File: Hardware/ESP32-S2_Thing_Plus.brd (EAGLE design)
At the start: 22.9 x 66 mm, 121 parts, among them J3 QWIIC_RA, J5 USB-C, J6 JTAG, Q1 2.5A/30V, Q2 MBT3904DW1T1, U1 MCP73831, U2 ESP32-S2-WROOM, U3 AP2112K-3.3V, U4 CP210X, Y1 32.768kHz

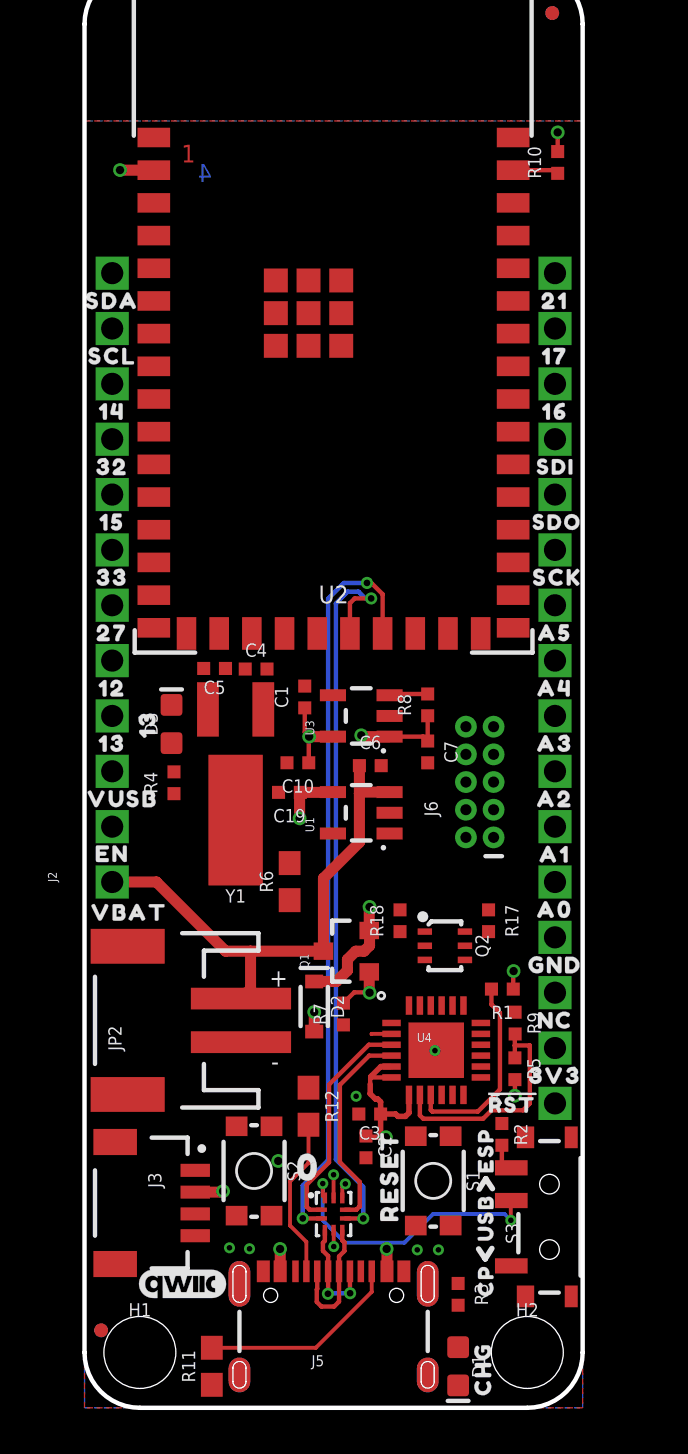
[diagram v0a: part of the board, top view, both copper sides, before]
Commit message: added charge current jumper options and did a bunch of routing
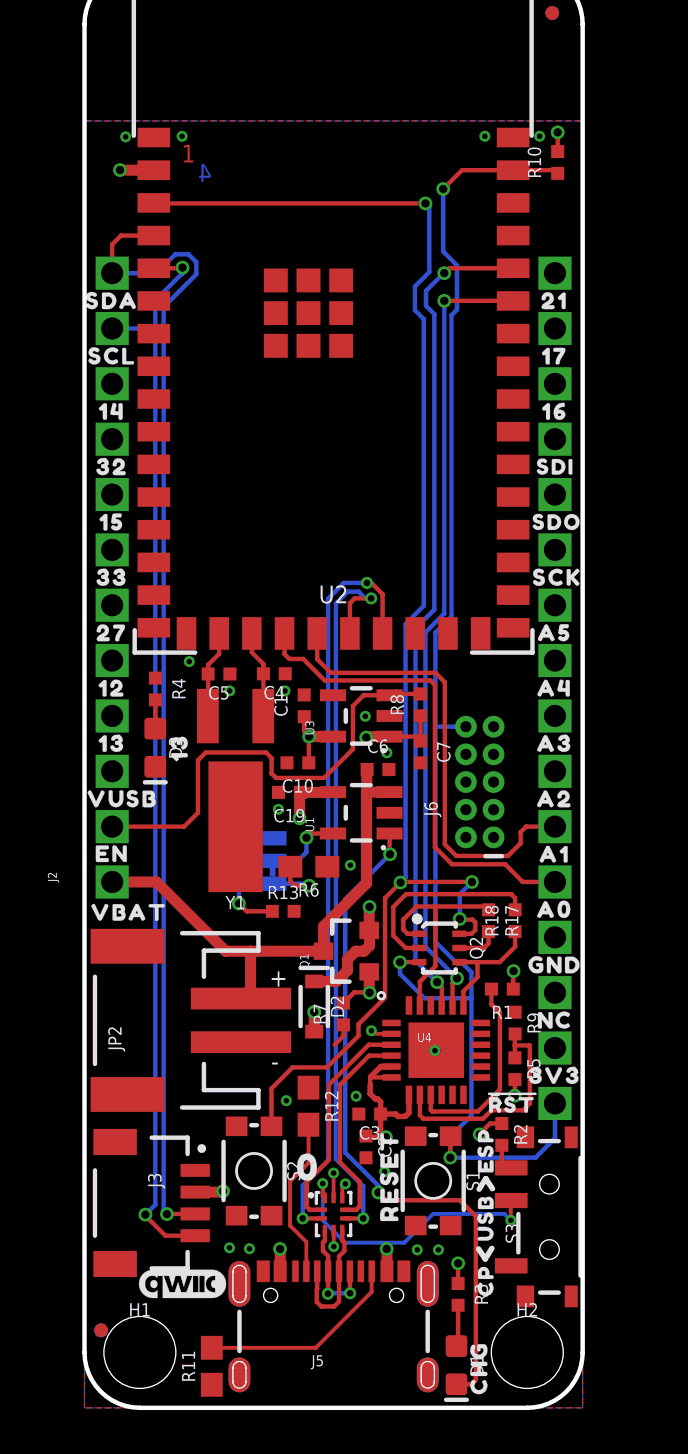
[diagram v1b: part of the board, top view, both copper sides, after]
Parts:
- added CHG: (no value), SparkFun-Jumpers:SMT-JUMPER_3_1-NC_TRACE_SILK
- added R13: 10k, SparkFun-Resistors:0402-TIGHT
- TP1: value TEST-POINTTP_15TH_THRU -> (none)
- moved TP1 15.6 mm to (17.8, 24.1)
- moved R18 5.28 mm to (19.8, 22.4)
- moved R4 4.38 mm to (3.26, 33.0), turned to 270 degrees
- moved U$74 1.82 mm to (4.36, 30.3)
- moved D3 1.32 mm to (3.25, 30.3), turned to 270 degrees
- moved R6 1.12 mm to (10.3, 24.8), turned to 180 degrees
- moved C4 0.87 mm to (8.71, 33.7), turned to 180 degrees
- moved C1 0.41 mm to (10.1, 32.2)
- moved C6 0.40 mm to (13.5, 29.3)
- moved C7 0.33 mm to (15.4, 30.1)
- moved R8 0.33 mm to (15.4, 32.3)
- moved C5 0.33 mm to (6.17, 33.7)
- moved Y1 0.30 mm to (6.93, 31.7)
- moved Q2 0.27 mm to (16.3, 21.1)
- moved U$78 0.18 mm to (18.1, 1.83)
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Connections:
- removed net N$14: R6.2, U1.5
- new net N$11: CHG.1, R13.1
- new net N$13: CHG.3, R6.2
- new net N$9: CHG.2, U1.5
- net GND: now also R13.2
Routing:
- net 0: track 0.00 -> 66.3 mm, vias 0 -> 3
- net CHIP_PU: track 2.10 -> 66.4 mm, vias 0 -> 3
- net SDA: track 0.00 -> 53.4 mm, vias 0 -> 1
- net SCL: track 0.00 -> 50.2 mm, vias 0 -> 2
- net TX: track 0.00 -> 38.2 mm, vias 0 -> 2
- net RX: track 0.00 -> 36.5 mm, vias 0 -> 2
- net CHG: track 0.00 -> 31.4 mm, vias 0 -> 2
- net A0: track 0.00 -> 22.1 mm
- net A1: track 0.00 -> 21.0 mm
- net EN: track 1.77 -> 20.6 mm
- net DTR: track 0.00 -> 10.3 mm
- net N$12: track 0.00 -> 9.19 mm
- net V_USB: track 14.4 -> 20.5 mm, vias 6 -> 7
- net N$11: track 0.00 -> 5.88 mm, vias 0 -> 1
- net RTS: track 0.00 -> 5.80 mm
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
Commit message: Moved to smaller/newer 32.768kHz crystal
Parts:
- C4, C5: value 22pF -> 15pF
- Y1: device SparkFun-Clocks:CRYSTAL-SMD-2X6-CYL -> SparkFun-Clocks:CRYSTAL-SMD-3.2X1.5MM
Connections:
- net N$7: now also Y1.P$2; no longer Y1.X2
- net N$8: now also Y1.P$1; no longer Y1.X1
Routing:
- net EN: track 20.6 -> 17.8 mm
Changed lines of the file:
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@@
 <setting verticaltext="up"/>
 </settings>
-<grid distance="0.05" unitdist="inch" unit="inch" style="lines" multiple="1" display="yes" altdistance="0.001" altunitdist="inch" altunit="inch"/>
+<grid distance="0.05" unitdist="inch" unit="inch" style="lines" multiple="1" display="yes" altdistance="0.005" altunitdist="inch" altunit="inch"/>
 <layers>
 <layer number="1" name="Top" color="4" fill="1" visible="yes" active="yes"/>
 <layer number="2" name="Route2" color="1" fill="3" visible="no" active="yes"/>
 <layer number="15" name="Route15" color="4" fill="6" visible="no" active="yes"/>
-<layer number="16" name="Bottom" color="1" fill="1" visible="yes" active="yes"/>
+<layer number="16" name="Bottom" color="1" fill="1" visible="no" active="yes"/>
 <layer number="17" name="Pads" color="2" fill="1" visible="yes" active="yes"/>
 <layer number="18" name="Vias" color="2" fill="1" visible="yes" active="yes"/>
 <layer number="19" name="Unrouted" color="6" fill="1" visible="yes" active="yes"/>
 <layer number="20" name="Dimension" color="24" fill="1" visible="yes" active="yes"/>
-<layer number="21" name="tPlace" color="16" fill="1" visible="no" active="yes"/>
+<layer number="21" name="tPlace" color="16" fill="1" visible="yes" active="yes"/>
 <layer number="22" name="bPlace" color="14" fill="1" visible="no" active="yes"/>
 <layer number="23" name="tOrigins" color="15" fill="1" visible="yes" active="yes"/>
@@
 <layer number="47" name="Measures" color="7" fill="1" visible="no" active="yes"/>
 <layer number="48" name="Document" color="7" fill="1" visible="no" active="yes"/>
-<layer number="49" name="Reference" color="7" fill="1" visible="yes" active="yes"/>
-<layer number="51" name="tDocu" color="6" fill="1" visible="no" active="yes"/>
+<layer number="49" name="Reference" color="7" fill="1" visible="no" active="yes"/>
+<layer number="51" name="tDocu" color="6" fill="1" visible="yes" active="yes"/>
 <layer number="52" name="bDocu" color="7" fill="1" visible="no" active="yes"/>
 <layer number="3" name="Route3" color="4" fill="3" visible="no" active="no"/>
@@
 <attribute name="VALUE" x="22.733" y="8.763" size="0.6096" layer="27" font="vector" ratio="20" rot="R90" align="top-center"/>
 </element>
-<element name="Y1" library="SparkFun-Clocks" package="CRYSTAL-SMD-2X6-CYL" value="32.768kHz" x="6.934196875" y="31.74491875" smashed="yes" rot="R180">
+<element name="Y1" library="SparkFun-Clocks" package="CRYSTAL-SMD-3.2X1.5MM" value="32.768kHz" x="6.934196875" y="31.74491875" smashed="yes" rot="R180">
 <attribute name="NAME" x="6.934196875" y="23.48991875" size="0.6096" layer="25" font="vector" ratio="20" rot="R180" align="bottom-center"/>
-<attribute name="PROD_ID" value="XTAL-07894" x="6.934196875" y="31.74491875" size="1.778" layer="27" font="vector" ratio="15" rot="R180" display="off"/>
+<attribute name="PROD_ID" value="XTAL-13062" x="6.934196875" y="31.74491875" size="1.778" layer="27" font="vector" ratio="15" rot="R180" display="off"/>
 <attribute name="VALUE" x="6.934196875" y="33.26891875" size="0.6096" layer="27" font="vector" ratio="20" rot="R180" align="top-center"/>
 </element>
@@
 <attribute name="VALUE" value="10k" x="18.5896" y="12.5476" size="0.6096" layer="27" font="vector" ratio="20" rot="R270" align="top-center"/>
 </element>
-<element name="C4" library="SparkFun-Capacitors" package="0402-TIGHT" value="22pF" x="8.712203125" y="33.68548125" smashed="yes" rot="R180">
+<element name="C4" library="SparkFun-Capacitors" package="0402-TIGHT" value="15pF" x="8.712203125" y="33.68548125" smashed="yes" rot="R180">
 <attribute name="NAME" x="8.712203125" y="33.12348125" size="0.6096" layer="25" font="vector" ratio="20" rot="R180" align="bottom-center"/>
-<attribute name="PROD_ID" value="CAP-14674" x="8.712203125" y="33.68548125" size="1.778" layer="27" font="vector" ratio="15" rot="R180" display="off"/>
-<attribute name="VALUE" x="8.712203125" y="34.24748125" size="0.6096" layer="27" font="vector" ratio="20" rot="R180" align="top-center"/>
-</element>
-<element name="C5" library="SparkFun-Capacitors" package="0402-TIGHT" value="22pF" x="6.172196875" y="33.67531875" smashed="yes" rot="R180">
+<attribute name="PROD_ID" value="CAP-13063" x="8.712203125" y="33.68548125" size="1.778" layer="27" font="vector" ratio="15" rot="R180" display="off"/>
+<attribute name="VALUE" value="15pF" x="8.712203125" y="34.24748125" size="0.6096" layer="27" font="vector" ratio="20" rot="R180" align="top-center"/>
+</element>
+<element name="C5" library="SparkFun-Capacitors" package="0402-TIGHT" value="15pF" x="6.172196875" y="33.67531875" smashed="yes" rot="R180">
 <attribute name="NAME" x="6.172196875" y="33.11331875" size="0.6096" layer="25" font="vector" ratio="20" rot="R180" align="bottom-center"/>
-<attribute name="PROD_ID" value="CAP-14674" x="6.172196875" y="33.67531875" size="1.778" layer="27" font="vector" ratio="15" rot="R180" display="off"/>
-<attribute name="VALUE" x="6.172196875" y="34.23731875" size="0.6096" layer="27" font="vector" ratio="20" rot="R180" align="top-center"/>
+<attribute name="PROD_ID" value="CAP-13063" x="6.172196875" y="33.67531875" size="1.778" layer="27" font="vector" ratio="15" rot="R180" display="off"/>
+<attribute name="VALUE" value="15pF" x="6.172196875" y="34.23731875" size="0.6096" layer="27" font="vector" ratio="20" rot="R180" align="top-center"/>
 </element>
 <element name="R11" library="SparkFun-Resistors" package="0603" value="5.1k" x="5.842" y="1.905" smashed="yes" rot="R90">
@@
 <wire x1="12.319" y1="32.2072" x2="12.319" y2="30.226" width="0.2032" layer="1"/>
 <wire x1="12.319" y1="30.226" x2="10.9982" y2="28.9052" width="0.2032" layer="1"/>
-<wire x1="8.7884" y1="28.9052" x2="8.5852" y2="29.1084" width="0.2032" layer="1"/>
-<wire x1="8.5852" y1="29.8196" x2="8.3312" y2="30.0736" width="0.2032" layer="1"/>
-<wire x1="8.3312" y1="30.0736" x2="5.5626" y2="30.0736" width="0.2032" layer="1"/>
-<wire x1="5.207" y1="29.718" x2="5.207" y2="27.305" width="0.2032" layer="1"/>
-<wire x1="5.207" y1="27.305" x2="4.572" y2="26.67" width="0.2032" layer="1"/>
-<wire x1="4.572" y1="26.67" x2="1.27" y2="26.67" width="0.2032" layer="1"/>
+<wire x1="2.286" y1="26.67" x2="1.27" y2="26.67" width="0.2032" layer="1"/>
 <wire x1="12.8118" y1="32.7" x2="12.319" y2="32.2072" width="0.2032" layer="1"/>
-<wire x1="10.9982" y1="28.9052" x2="8.7884" y2="28.9052" width="0.2032" layer="1"/>
-<wire x1="8.5852" y1="29.1084" x2="8.5852" y2="29.8196" width="0.2032" layer="1"/>
-<wire x1="5.5626" y1="30.0736" x2="5.207" y2="29.718" width="0.2032" layer="1"/>
+<wire x1="4.5212" y1="28.9052" x2="2.286" y2="26.67" width="0.2032" layer="1"/>
+<wire x1="10.9982" y1="28.9052" x2="4.5212" y2="28.9052" width="0.2032" layer="1"/>
 </signal>
 <signal name="N$2">
@@
 <signal name="N$7">
 <contactref element="U2" pad="18"/>
-<contactref element="Y1" pad="X2"/>
+<contactref element="Y1" pad="P$2"/>
 <contactref element="C5" pad="2"/>
 <wire x1="6.18" y1="35.535" x2="6.18" y2="34.6026" width="0.2032" layer="1"/>
@@
 <wire x1="6.18" y1="34.6026" x2="5.672196875" y2="34.094796875" width="0.2032" layer="1"/>
 <wire x1="5.672196875" y1="33.67531875" x2="5.672196875" y2="31.75291875" width="0.2032" layer="1"/>
-<wire x1="5.672196875" y1="31.75291875" x2="5.664196875" y2="31.74491875" width="0.2032" layer="1"/>
+<wire x1="5.672196875" y1="31.75291875" x2="5.684196875" y2="31.74491875" width="0" layer="19" extent="1-1"/>
 </signal>
 <signal name="N$8">
 <contactref element="U2" pad="19"/>
-<contactref element="Y1" pad="X1"/>
+<contactref element="Y1" pad="P$1"/>
 <contactref element="C4" pad="2"/>
 <wire x1="7.68" y1="35.535" x2="7.68" y2="34.6618" width="0.2032" layer="1"/>
@@
 <wire x1="7.68" y1="34.6618" x2="8.212203125" y2="34.129596875" width="0.2032" layer="1"/>
 <wire x1="8.212203125" y1="33.68548125" x2="8.212203125" y2="31.752925" width="0.2032" layer="1"/>
-<wire x1="8.212203125" y1="31.752925" x2="8.204196875" y2="31.74491875" width="0.2032" layer="1"/>
+<wire x1="8.212203125" y1="31.752925" x2="8.184196875" y2="31.74491875" width="0" layer="19" extent="1-1"/>
 </signal>
 <signal name="CC2">

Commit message: moving vreg in progress
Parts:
- moved R8 14.0 mm to (3.00, 25.8), turned to 270 degrees
- moved C7 11.7 mm to (5.49, 24.0), turned to 180 degrees
- moved U3 8.92 mm to (5.87, 26.0), turned to 270 degrees
- moved C1 5.54 mm to (5.77, 28.7), turned to 0 degrees
- moved C10 4.02 mm to (5.78, 29.8), turned to 0 degrees
- moved C19 1.81 mm to (10.9, 29.3)
- moved R13 1.20 mm to (10.3, 23.1)
- moved CHG 0.41 mm to (9.04, 25.1)
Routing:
- net EN: track 17.8 -> 4.59 mm
- net VIN: track 16.9 -> 20.5 mm
- net 3.3V: track 29.7 -> 26.5 mm
- net V_BATT: track 23.6 -> 26.6 mm
- net GND: vias 22 -> 23

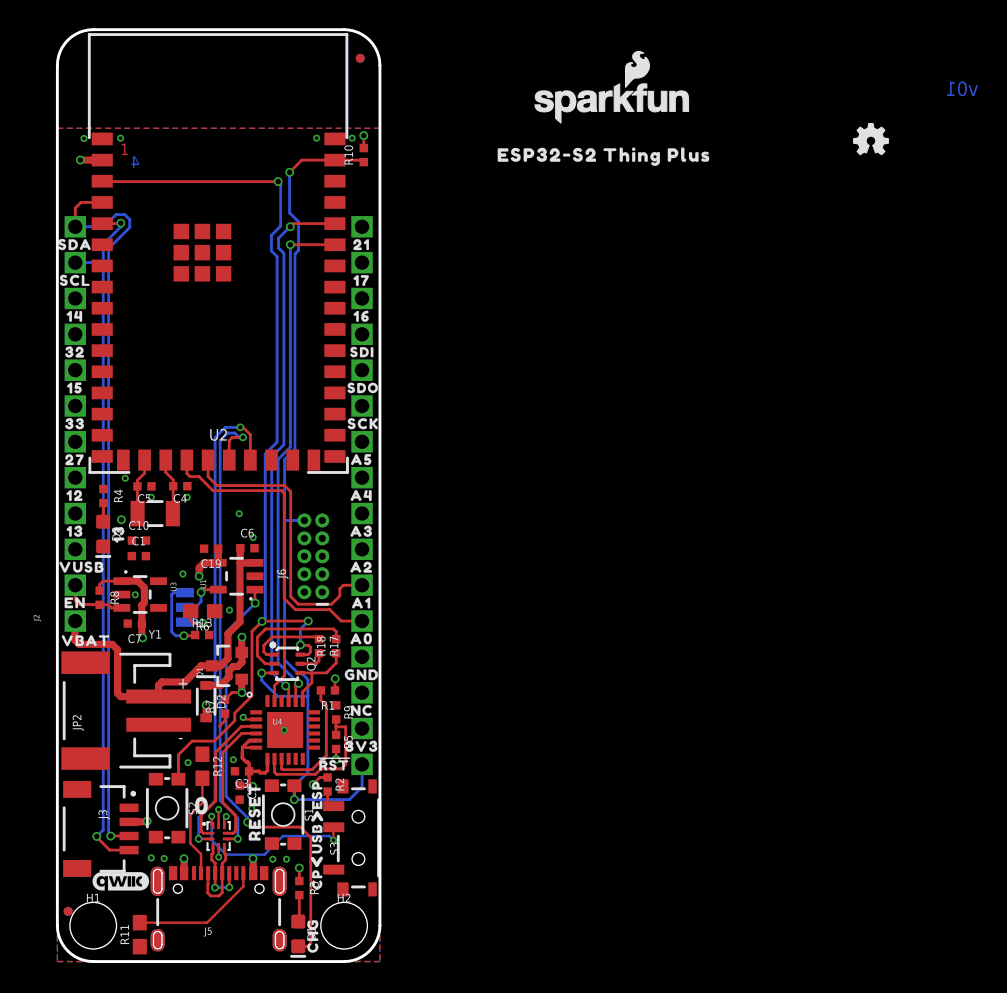
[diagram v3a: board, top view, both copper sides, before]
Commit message: All IO (except "extra SMD IO") routed
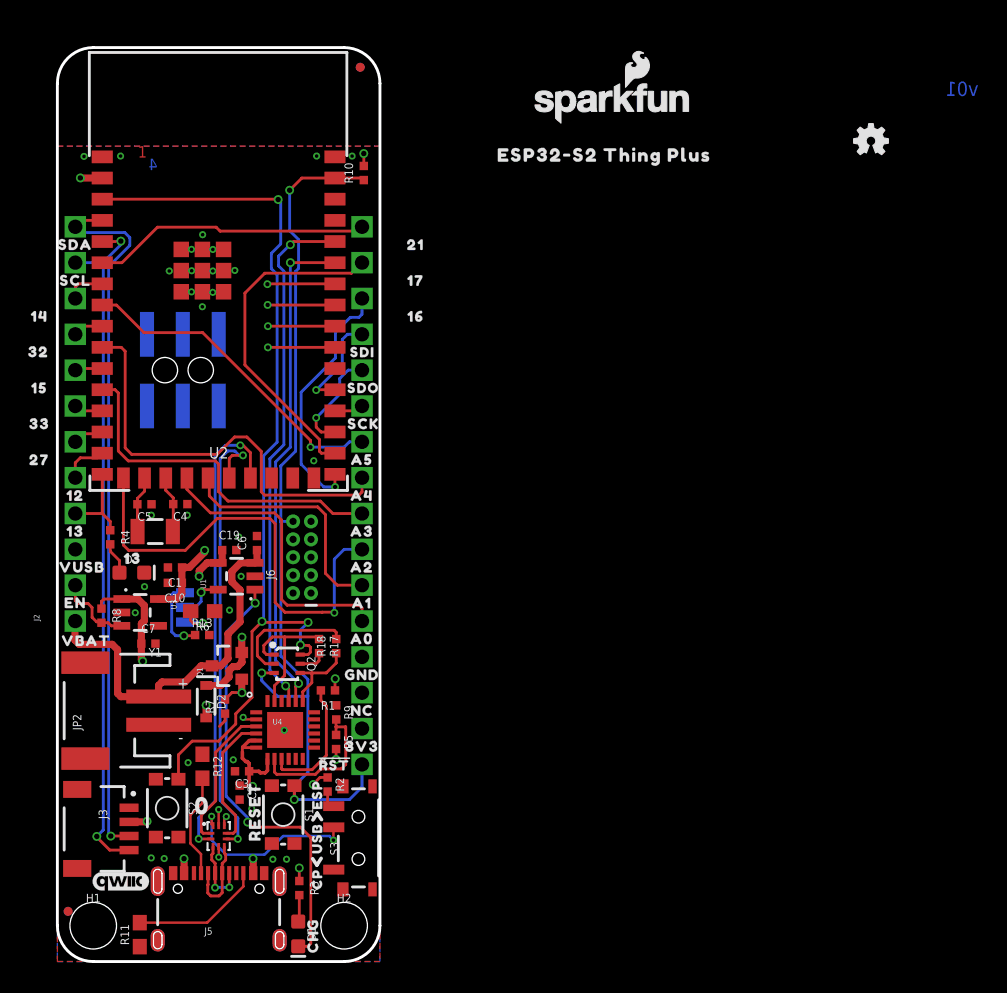
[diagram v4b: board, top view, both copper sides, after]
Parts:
- added J1: (no value), SparkFun-Connectors:2X3_SMT_POSTS
- moved U$31 8.89 mm to (-7.11, 52.1)
- moved U$33 8.89 mm to (-7.11, 49.5)
- moved U$4 8.89 mm to (30.0, 49.5)
- moved U$5 8.89 mm to (30.0, 47.0)
- moved U$3 6.35 mm to (27.4, 52.1)
- moved U$34 5.08 mm to (-3.30, 47.0)
- moved U$35 5.08 mm to (-3.30, 44.5)
- moved U$36 5.08 mm to (-3.30, 41.9)
- moved U$37 5.08 mm to (-3.30, 39.4)
- moved U$38 5.08 mm to (-3.30, 36.8)
- moved C10 3.93 mm to (8.32, 26.8), turned to 180 degrees
- moved U$93 3.81 mm to (25.4, 45.7)
- moved U$94 3.81 mm to (25.4, 48.3)
- moved U$95 3.81 mm to (25.4, 50.8)
- moved D3 3.41 mm to (5.28, 27.6), turned to 0 degrees
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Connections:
- new net 10: J2.7, U2.13
- new net 11: J2.6, U2.14
- new net 12: J2.5, U2.15
- new net 21: U2.24
- new net 26: U2.25
- new net 3: J4.16, U2.6
- new net 33: J4.14, U2.27
- new net 34: J4.15, U2.28
- new net 38: U2.32
- new net 4: J2.10, U2.7
- new net 45: U2.39
- new net 46: U2.40
- new net 6: J2.9, U2.9
- new net 8: J2.8, U2.11
- new net N$14: J1.2
- new net N$15: J1.4
- new net N$16: J1.6
- new net N$18: J1.1
- new net N$19: J1.3
- new net N$20: J1.5
- net 13: now also J2.4, U2.16
- net A2: now also U2.17
- net A3: now also U2.12
- net A4: now also U2.10
- net A5: now also U2.8
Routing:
- net A2: track 0.00 -> 32.9 mm, vias 0 -> 1
- net A4: track 0.00 -> 30.6 mm
- net MTMS: track 0.00 -> 28.0 mm, vias 0 -> 1
- net A3: track 0.00 -> 25.6 mm
- net 34: track 0.00 -> 23.7 mm
- net A5: track 0.00 -> 23.0 mm, vias 0 -> 1
- net MTDI: track 0.00 -> 22.1 mm, vias 0 -> 1
- net MTDO: track 0.00 -> 21.9 mm, vias 0 -> 1
- net MTCK: track 0.00 -> 21.6 mm, vias 0 -> 1
- net 3: track 0.00 -> 19.7 mm
- net 33: track 0.00 -> 17.9 mm, vias 0 -> 1
- net COPI: track 0.00 -> 7.43 mm, vias 0 -> 1
- net CIPO: track 0.00 -> 7.24 mm, vias 0 -> 1
- net 13: track 0.00 -> 6.19 mm
- net 3.3V: track 26.5 -> 32.3 mm
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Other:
- board size 22.9 x 66 mm -> 22.9 x 64.8 mm
